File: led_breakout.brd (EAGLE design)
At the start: 8.3 x 9.5 mm, 4 parts

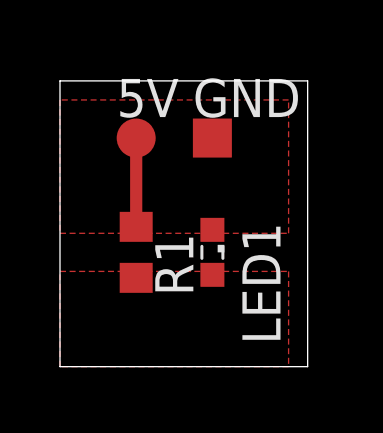
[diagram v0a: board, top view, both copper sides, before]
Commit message: tighter package
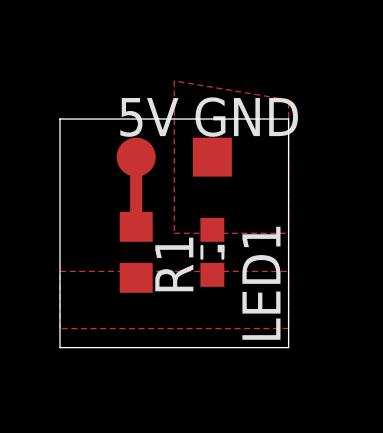
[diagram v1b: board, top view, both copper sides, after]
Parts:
- moved 5V 0.63 mm to (2.54, 6.99)
- moved GND 0.63 mm to (5.08, 6.99)
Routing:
- net 5V: track 2.96 -> 2.33 mm
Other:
- board size 8.3 x 9.5 mm -> 7.6 x 7.6 mm
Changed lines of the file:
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@@
 <setting verticaltext="up"/>
 </settings>
-<grid distance="25" unitdist="mil" unit="mm" style="lines" multiple="1" display="yes" altdistance="0.025" altunitdist="inch" altunit="inch"/>
+<grid distance="25" unitdist="mil" unit="mil" style="lines" multiple="1" display="yes" altdistance="0.025" altunitdist="inch" altunit="inch"/>
 <layers>
 <layer number="1" name="Top" color="4" fill="1" visible="yes" active="yes"/>
@@
 <board>
 <plain>
-<wire x1="0" y1="0" x2="8.255" y2="0" width="0" layer="20"/>
-<wire x1="8.255" y1="0" x2="8.255" y2="9.525" width="0" layer="20"/>
-<wire x1="8.255" y1="9.525" x2="0" y2="9.525" width="0" layer="20"/>
-<wire x1="0" y1="9.525" x2="0" y2="0" width="0" layer="20"/>
+<wire x1="0" y1="0.635" x2="7.62" y2="0.635" width="0" layer="20"/>
+<wire x1="7.62" y1="0.635" x2="7.62" y2="8.255" width="0" layer="20"/>
+<wire x1="7.62" y1="8.255" x2="0" y2="8.255" width="0" layer="20"/>
+<wire x1="0" y1="8.255" x2="0" y2="0.635" width="0" layer="20"/>
 </plain>
 <attributes>
@@
 <element name="R1" library="rcl" package="R0603" value="220" x="2.54" y="3.81" rot="R270"/>
 <element name="LED1" library="led" package="SML0603" value="" x="5.08" y="3.81" rot="R270"/>
-<element name="5V" library="testpad" package="TP13R" value="TPTP13R" x="2.54" y="7.62">
-<attribute name="TP_SIGNAL_NAME" value="" x="17.78" y="-7.62" size="1.778" layer="27" display="off"/>
+<element name="5V" library="testpad" package="TP13R" value="TPTP13R" x="2.54" y="6.985">
+<attribute name="TP_SIGNAL_NAME" value="" x="17.78" y="-8.255" size="1.778" layer="27" display="off"/>
 </element>
-<element name="GND" library="testpad" package="TP13SQ" value="TPTP13SQ" x="5.08" y="7.62">
-<attribute name="TP_SIGNAL_NAME" value="" x="22.86" y="-3.81" size="1.778" layer="27" display="off"/>
+<element name="GND" library="testpad" package="TP13SQ" value="TPTP13SQ" x="5.08" y="6.985">
+<attribute name="TP_SIGNAL_NAME" value="" x="22.86" y="-4.445" size="1.778" layer="27" display="off"/>
 </element>
 </elements>
@@
 <vertex x="0" y="3.175"/>
 <vertex x="7.62" y="3.175"/>
-<vertex x="7.62" y="0"/>
-<vertex x="0" y="0"/>
+<vertex x="7.62" y="1.27"/>
+<vertex x="0" y="1.27"/>
 </polygon>
 </signal>
@@
 <contactref element="5V" pad="TP"/>
 <contactref element="R1" pad="1"/>
-<wire x1="2.54" y1="7.62" x2="2.54" y2="4.66" width="0.4064" layer="1"/>
+<wire x1="2.54" y1="6.985" x2="2.54" y2="4.66" width="0.4064" layer="1"/>
 </signal>
 <signal name="GND">
@@
 <contactref element="LED1" pad="C"/>
 <polygon width="0.4064" layer="1" isolate="0.4064">
-<vertex x="0" y="4.445"/>
+<vertex x="3.81" y="4.445"/>
 <vertex x="7.62" y="4.445"/>
 <vertex x="7.62" y="8.89"/>
-<vertex x="0" y="8.89"/>
+<vertex x="3.81" y="9.525"/>
 </polygon>
 </signal>
